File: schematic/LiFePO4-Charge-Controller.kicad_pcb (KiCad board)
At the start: 2 copper layers, 47 parts, among them IC1 PC817, IC2 PC817, IC3 PC817, P1 CONN_2, P2 CONN_4, P3 CONN_4, P4 CONN_4, P5 CONN_4, P6 CONN_4, P7 CONN_2, P8 CONN_2, P9 CONN_2, Q1 NPN, U1 AD8236, U2 SI8400, U3 SI8400, U4 ARDUINO_MINI, U5 SI8400

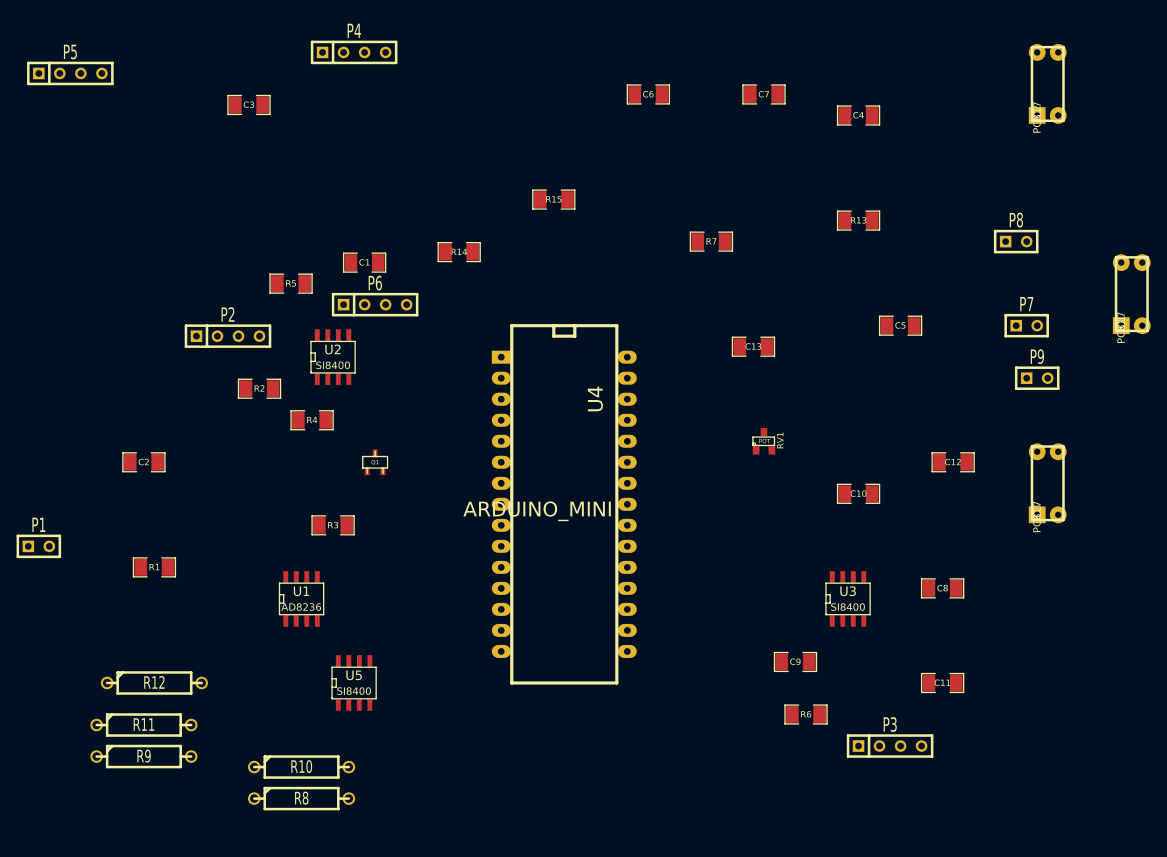
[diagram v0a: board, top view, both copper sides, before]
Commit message: Autoraouted board b4 contraction
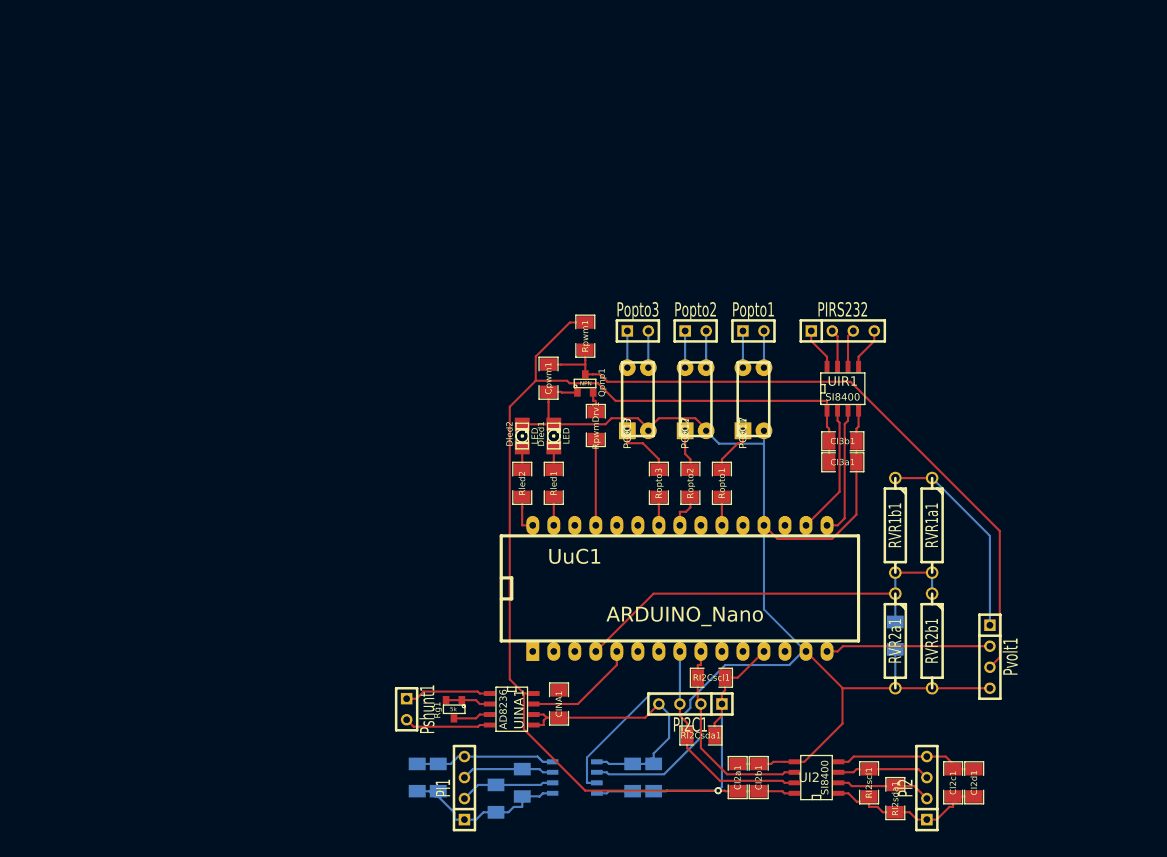
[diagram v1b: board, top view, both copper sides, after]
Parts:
- removed C1, C10, C11, C12, C13, C2, C3, C4, C5, C6, C7, C8, C9: C, SM1206
- removed IC1, IC2, IC3: PC817, DIP-4
- removed P1, P7, P8, P9: CONN_2, SIL-2
- removed P2, P3, P4, P5, P6: CONN_4, SIL-4
- removed Q1: NPN, sot23
- removed R1, R13, R14, R15, R2, R3, R4, R5, R6, R7: R, SM1206
- removed R10, R8: 99k, R4-5
- removed R11, R9: 1k, R4-5
- removed R12: 560, R4-5
- removed RV1: POT, SOT23
- removed U1: AD8236, SO8E
- removed U2, U3, U5: SI8400, SO8E
- removed U4: ARDUINO_MINI, arduino_mini
- added CI1a1: 100nF, SM1206, B.Cu at (203.8, 160.0)
- added CI1b1: 1uF, SM1206, B.Cu at (201.3, 160.0)
- added CI1c1: 100nF, SM1206, B.Cu at (175.3, 160.0)
- added CI1d1: 1uF, SM1206, B.Cu at (177.8, 160.0)
- added CI2a1: 100nF, SM1206, F.Cu at (214.0, 160.0)
- added CI2b1: 1uF, SM1206, F.Cu at (216.5, 160.0)
- added CI2c1: 100nF, SM1206, F.Cu at (240.0, 160.7)
- added CI2d1: 1uF, SM1206, F.Cu at (242.6, 160.7)
- added CI3a1: 100nF, SM1206, F.Cu at (226.7, 121.9)
- added CI3b1: 1uF, SM1206, F.Cu at (226.7, 119.4)
- added CINA1: 100nF, SM1206, F.Cu at (192.4, 151.1)
- added CV1: 10pF, SM1206, B.Cu at (233.0, 142.9)
- added Cpwm1: 300nF, SM1206, F.Cu at (191.1, 111.8)
- added Dled1: LED, LED-1206, F.Cu at (191.8, 118.7)
- added Dled2: LED, LED-1206, F.Cu at (188.0, 118.7)
- added OC1: PC817, DIP-4, F.Cu at (214.6, 118.1)
- added OC2: PC817, DIP-4, F.Cu at (207.6, 118.1)
- added OC3: PC817, DIP-4, F.Cu at (200.7, 118.1)
- added PI1: I2C, SIL-4, F.Cu at (181.0, 161.3)
- added PI2: I2C, SIL-4, F.Cu at (236.9, 161.3)
- added PI2C1: I2C, SIL-4, F.Cu at (208.3, 151.1)
- added PIRS232: RS232, SIL-4, F.Cu at (226.7, 106.0)
- added Popto1: opto, SIL-2, F.Cu at (215.9, 106.0)
- added Popto2: opto, SIL-2, F.Cu at (208.9, 106.0)
- added Popto3: opto, SIL-2, F.Cu at (201.9, 106.0)
- added Pshunt1: differential, SIL-2, F.Cu at (174.0, 151.8)
- added Pvolt1: Gnd PWM 12V B+, SIL-4, F.Cu at (244.5, 145.4)
- added Qpnp1: NPN, SOT23, F.Cu at (195.6, 112.4)
- added RI1scl1: 5k, SM1206, B.Cu at (188.0, 160.7)
- added RI1sda1: 5k, SM1206, B.Cu at (184.8, 162.6)
- added RI2Cscl1: 1.8k, SM1206, F.Cu at (210.8, 148.0)
- added RI2Csda1: 1.8k, SM1206, F.Cu at (209.6, 154.9)
- added RI2scl1: 5k, SM1206, F.Cu at (229.9, 160.7)
- added RI2sda1: 5k, SM1206, F.Cu at (233.0, 162.6)
- added RVR1a1: 99k, R4-5, F.Cu at (237.5, 129.5)
- added RVR1b1: 99k, R4-5, F.Cu at (233.0, 129.5)
- added RVR2a1: 1k, R4-5, F.Cu at (233.0, 143.5)
- added RVR2b1: 1k, R4-5, F.Cu at (237.5, 143.5)
- added Rg1: 5k, SOT23, F.Cu at (179.7, 151.8)
- added Rled1: 1k, SM1206, F.Cu at (191.8, 124.5)
- added Rled2: 1K, SM1206, F.Cu at (188.0, 124.5)
- added Ropto1: 1k, SM1206, F.Cu at (212.1, 124.5)
- added Ropto2: 1k, SM1206, F.Cu at (208.3, 124.5)
- added Ropto3: 1k, SM1206, F.Cu at (204.5, 124.5)
- added Rpwm1: 120, SM1206, F.Cu at (195.6, 106.7)
- added RpwmDrv1: 560, SM1206, F.Cu at (196.8, 117.5)
- added UI1: SI8400, SO8E, B.Cu at (194.3, 160.0)
- added UI2: SI8400, SO8E, F.Cu at (223.5, 160.0)
- added UINA1: AD8236, SO8E, F.Cu at (186.7, 151.8)
- added UIR1: SI8400, SO8E, F.Cu at (226.7, 113.0)
- added UuC1: ARDUINO_Nano, arduino_mini, F.Cu at (208.3, 137.2)
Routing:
- net Gnd: track 0.00 -> 196.0 mm
- net 5v: track 0.00 -> 174.5 mm, vias 0 -> 1
- net N-000008: track 0.00 -> 82.3 mm
- net N-000009: track 0.00 -> 52.0 mm
- net N-0000057: track 0.00 -> 45.4 mm
- net N-0000056: track 0.00 -> 43.5 mm
- net N-0000059: track 0.00 -> 25.1 mm
- net N-0000040: track 0.00 -> 21.0 mm
- net N-0000039: track 0.00 -> 20.8 mm
- net N-0000037: track 0.00 -> 19.9 mm
- net N-0000013: track 0.00 -> 17.9 mm
- net N-000003: track 0.00 -> 17.0 mm
- net N-000002: track 0.00 -> 15.6 mm
- net N-000001: track 0.00 -> 15.6 mm
- net N-0000038: track 0.00 -> 13.6 mm
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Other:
- net class Default: clearance 0.254 -> 0.3675
- rule trace_clearance: 0.254 -> 0.3675

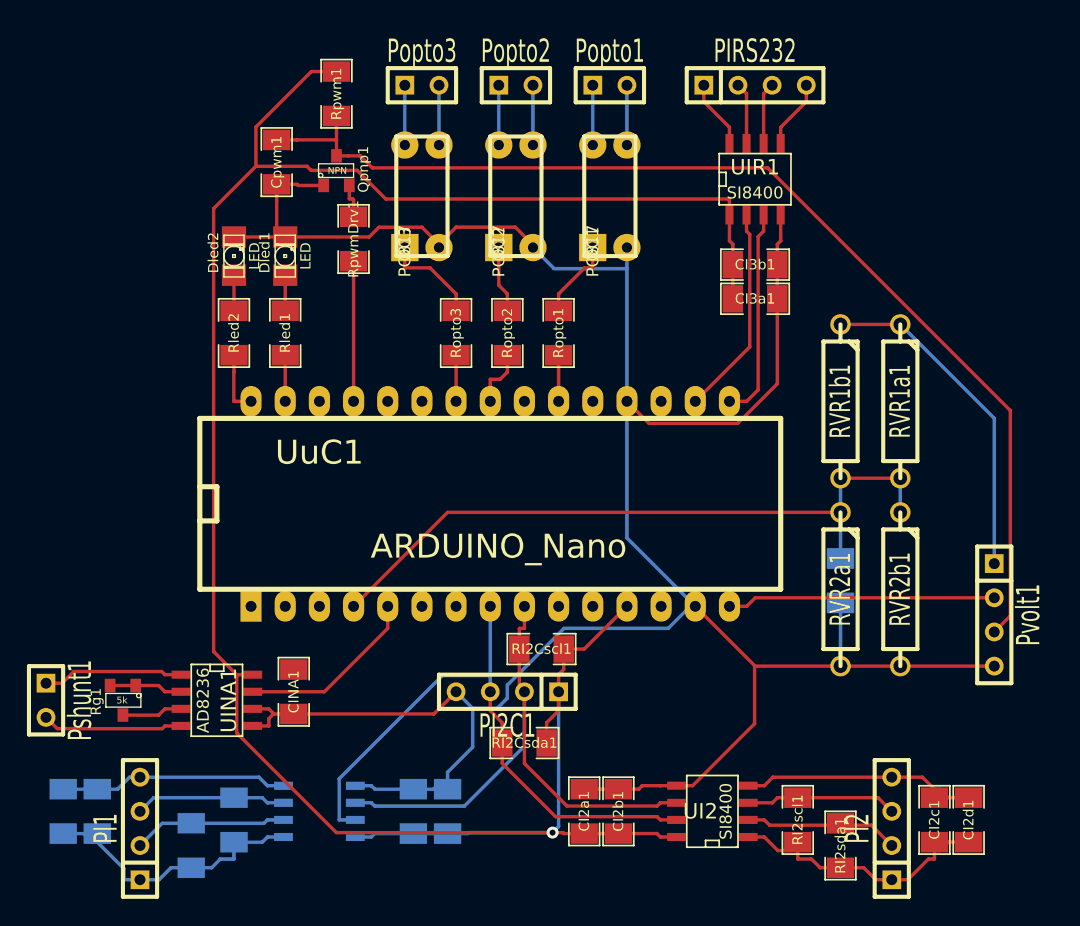
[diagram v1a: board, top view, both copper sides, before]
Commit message: Smaller, w solid fill
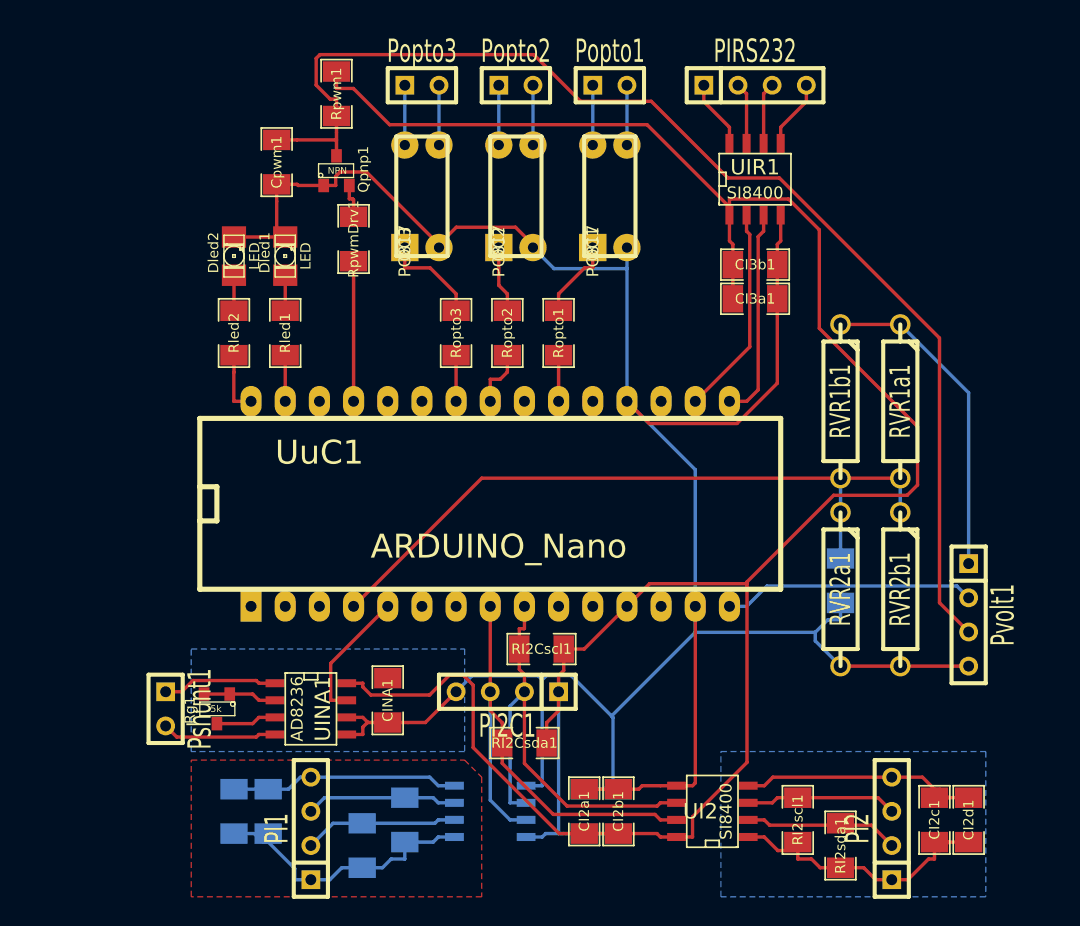
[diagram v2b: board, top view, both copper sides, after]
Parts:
- moved CI1b1 12.7 mm to (214.0, 160.0)
- moved CI1c1 12.7 mm to (188.0, 160.0)
- moved PI1 12.7 mm to (193.7, 161.3)
- moved RI1sda1 12.7 mm to (197.5, 162.6)
- moved CI1a1 12.7 mm to (216.5, 160.0)
- moved CI1d1 12.7 mm to (190.5, 160.0)
- moved RI1scl1 12.7 mm to (200.7, 160.7)
- moved UI1 12.7 mm to (207.0, 160.0)
- moved Pshunt1 8.91 mm to (182.9, 152.4)
- moved UINA1 7.01 mm to (193.7, 152.4)
- moved Rg1 7.01 mm to (186.7, 152.4)
- moved CINA1 7.01 mm to (199.4, 151.8)
- moved Pvolt1 1.91 mm to (242.6, 145.4)
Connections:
- net N-000003 renamed I2C1_GND
- CI2c1 pad 2: N-0000013 (its old number) -> I2C2_GND
- CI2d1 pad 2: N-0000013 (its old number) -> I2C2_GND
- PI2 pad 4: N-0000013 (its old number) -> I2C2_GND
- PIRS232 pad 4: N-0000010 (its old number) -> RS232_GND
- UI2 pad 4: N-0000013 (its old number) -> I2C2_GND
- UIR1 pad 5: N-0000010 (its old number) -> RS232_GND
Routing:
- net N-0000013 (its old number): track 17.9 -> 0.00 mm
- net I2C2_GND: track 0.00 -> 17.9 mm
- net N-0000057: track 43.5 -> 34.8 mm
- net N-0000022: track 82.3 -> 90.5 mm
- net 5v: track 174.5 -> 182.8 mm, vias 1 -> 0
- net N-0000053: track 45.4 -> 38.1 mm
- net RS232_GND: track 0.00 -> 5.11 mm
- net N-0000010 (its old number): track 5.11 -> 0.00 mm
- net N-0000034: track 13.6 -> 9.94 mm
- net Gnd: track 196.0 -> 193.4 mm
- net N-0000036: track 10.5 -> 8.56 mm
- net N-0000035: track 10.5 -> 8.55 mm
- net N-0000038: track 19.9 -> 18.8 mm
- net N-000007: track 52.0 -> 53.1 mm
- net N-0000059: track 25.1 -> 24.3 mm
- added copper zone on B.Cu, net Gnd
- added copper zone on F.Cu, net I2C1_GND
- added copper zone on B.Cu, net I2C2_GND

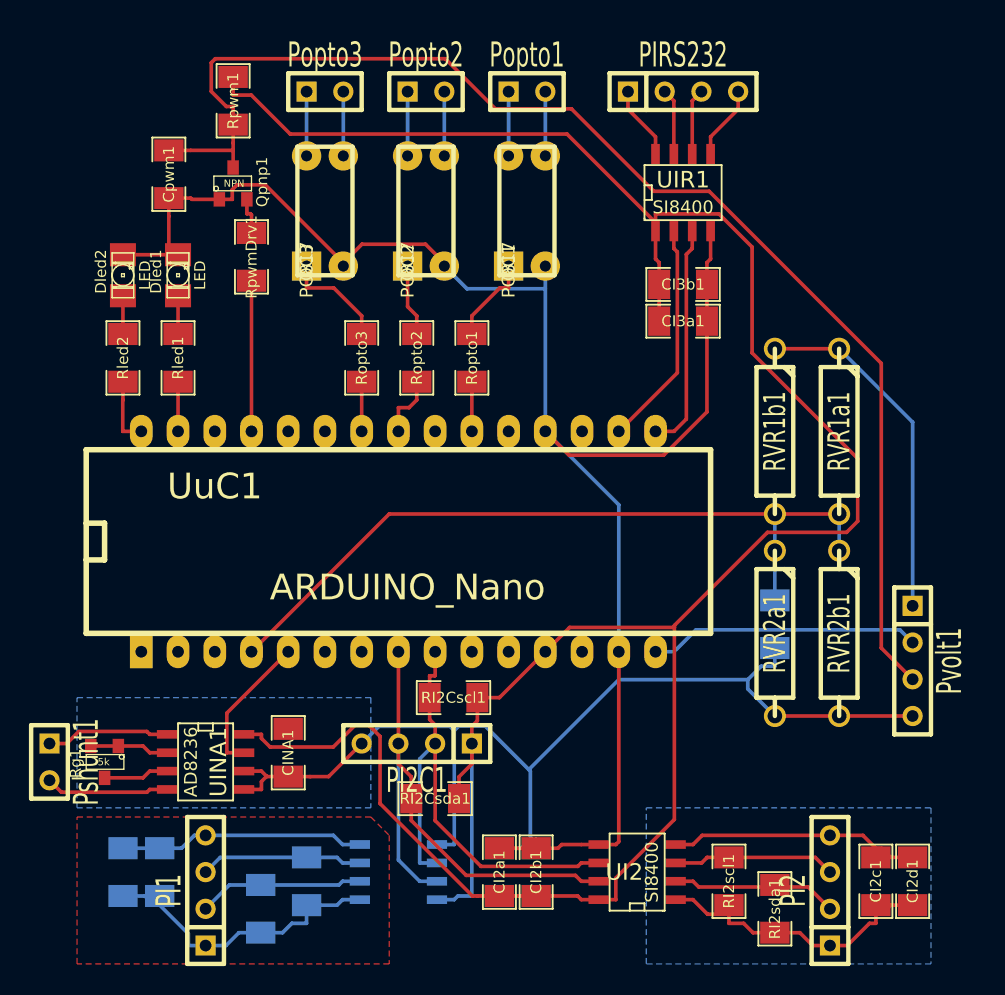
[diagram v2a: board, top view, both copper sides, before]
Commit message: PCB satisfactory, bit of a mess around I2C, but will go with it
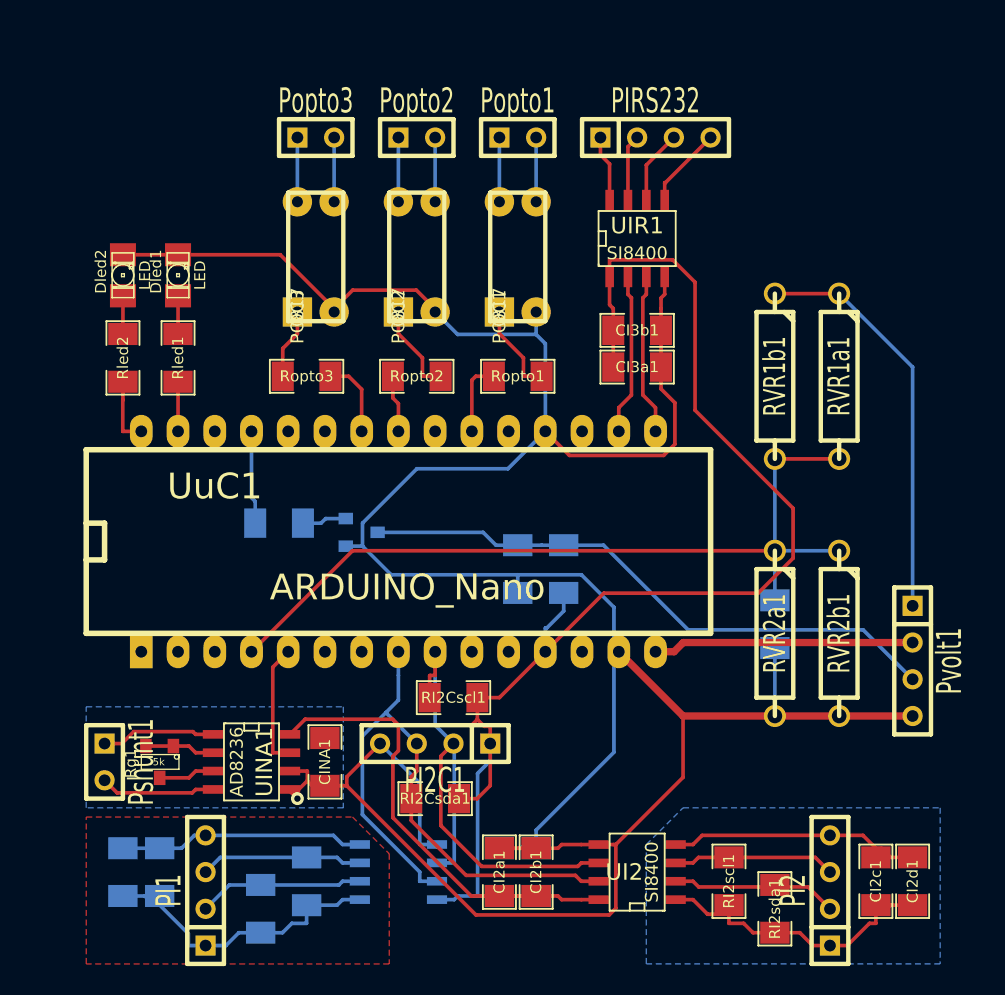
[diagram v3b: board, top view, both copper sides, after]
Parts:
- Cpwm1, Qpnp1, Rpwm1, RpwmDrv1: moved to B.Cu
- moved Rpwm1 39.6 mm to (218.4, 139.1), turned to 270 degrees
- moved Cpwm1 36.4 mm to (215.3, 139.1)
- moved Qpnp1 25.7 mm to (204.5, 136.5), turned to 90 degrees
- moved RpwmDrv1 18.5 mm to (198.8, 135.9), turned to 0 degrees
- moved CI3b1 4.49 mm to (223.5, 122.6)
- moved CI3a1 4.49 mm to (223.5, 125.1)
- moved UIR1 4.49 mm to (223.5, 116.2)
- moved Ropto3 4.02 mm to (200.7, 125.7), turned to 180 degrees
- moved Pshunt1 3.81 mm to (186.7, 152.4)
- moved Rg1 3.81 mm to (190.5, 152.4)
- moved RVR1a1 3.81 mm to (237.5, 125.7)
- moved RVR1b1 3.81 mm to (233.0, 125.7)
- moved PIRS232 3.70 mm to (224.8, 109.2)
- moved Ropto1 3.42 mm to (215.3, 125.7), turned to 0 degrees
- moved OC2 3.24 mm to (207.0, 121.3)
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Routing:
- net 5v: track 182.8 -> 130.4 mm
- net Gnd: track 193.4 -> 244.7 mm, vias 0 -> 1
- net N-0000022: track 90.5 -> 41.2 mm
- net N-0000053: track 38.1 -> 42.9 mm
- net N-000007: track 53.1 -> 57.8 mm
- net N-000002: track 15.6 -> 11.1 mm
- net N-000001: track 15.6 -> 11.1 mm
- net N-0000027: track 10.4 -> 6.46 mm
- net N-0000059: track 24.3 -> 28.1 mm
- net N-0000057: track 34.8 -> 38.1 mm
- net N-0000015: track 7.38 -> 4.87 mm
- net D6: track 3.43 -> 5.44 mm
- net D3: track 3.43 -> 5.18 mm
- net N-0000038: track 18.8 -> 20.2 mm
- net N-0000018: track 4.96 -> 6.39 mm
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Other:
- net class Power added: clearance 0.3675, trace_width 0.508, via_dia 0.889, via_drill 0.635
